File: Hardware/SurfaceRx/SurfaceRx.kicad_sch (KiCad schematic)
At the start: 29 parts, among them IC1 SC189ZSKTRT, J1 Conn_01x03, J2 Conn_01x03, J3 Conn_01x03, J4 Conn_01x03, J5 Conn_01x03, J6 Conn_01x03, J7 Conn_01x05, J8 Conn_01x03, P1 VDD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

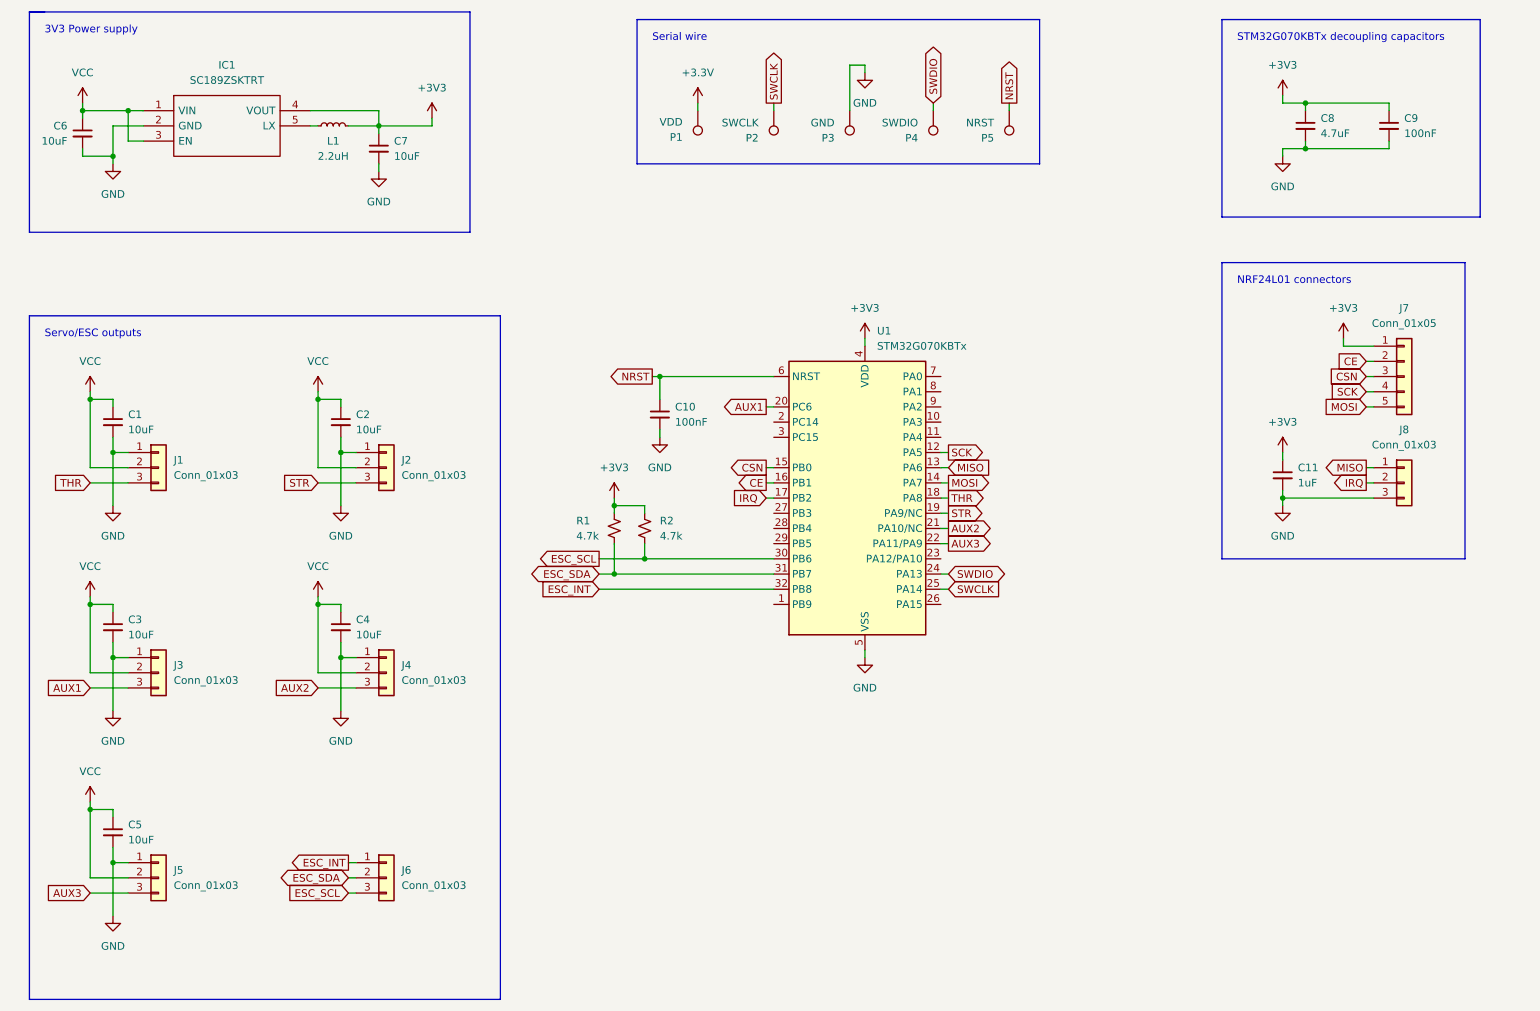
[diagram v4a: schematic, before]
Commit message: Added EEPROM to schematic
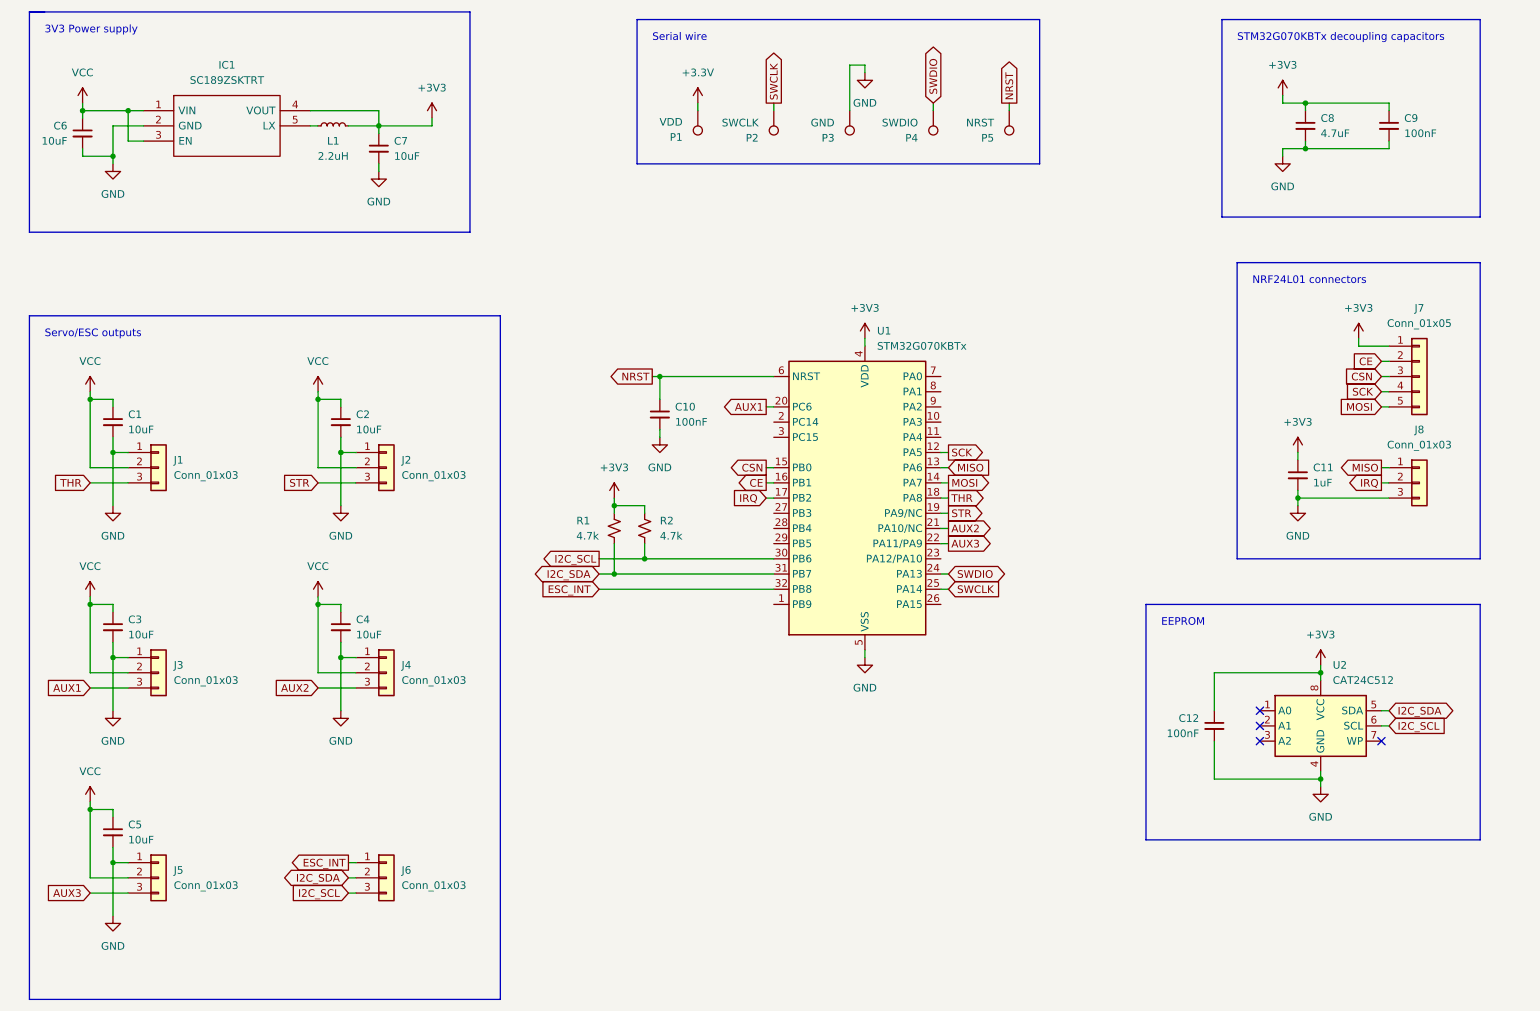
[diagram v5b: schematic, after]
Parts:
- added C12: 100nF, Capacitor_SMD:C_0603_1608Metric, symbol Device:C_Small
- added U2: CAT24C512, Package_SO:TSSOP-8_4.4x3mm_P0.65mm, symbol Custom_SurfaceRx:CAT24C512
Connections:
- net +3V3: now also C12.1, U2.8 (VCC)
- net GND: now also C12.2, U2.4 (GND)
- net ESC_SCL renamed I2C_SCL
- net I2C_SCL: now also U2.6 (SCL)
- net ESC_SDA renamed I2C_SDA
- net I2C_SDA: now also U2.5 (SDA)
- no-connect marks 0 -> 4
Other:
- note added: "EEPROM"
- moved on the sheet: C11, J7, J8

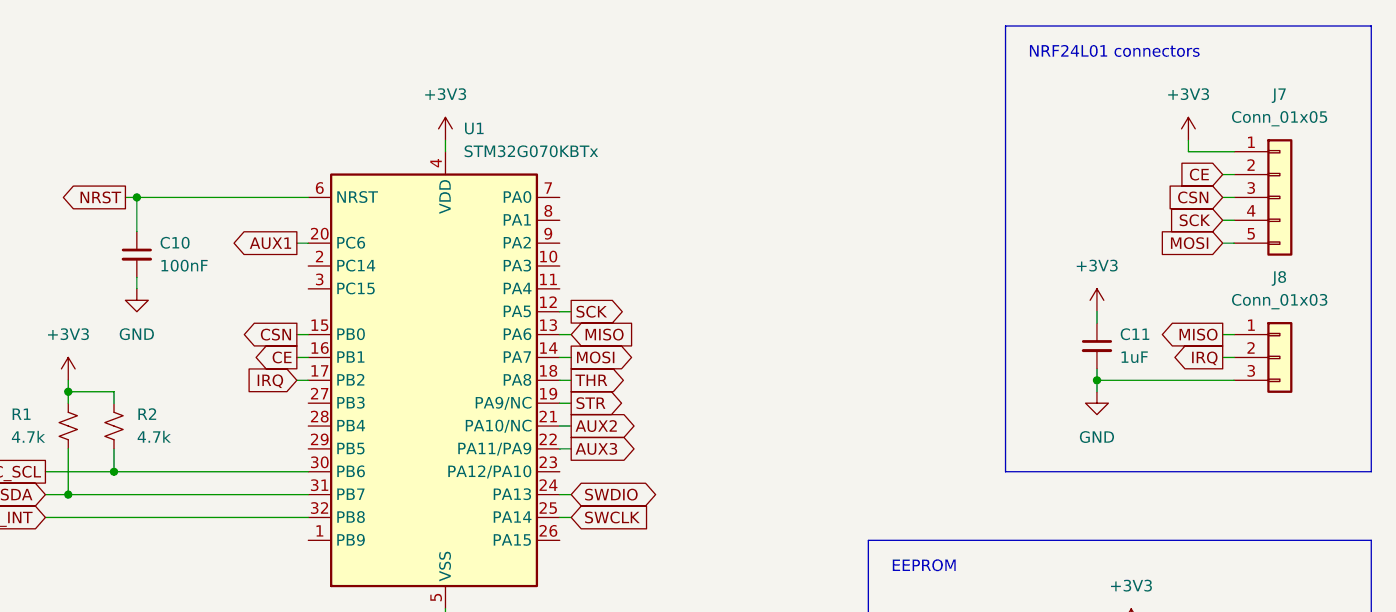
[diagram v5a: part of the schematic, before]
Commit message: Modified labels for clarity
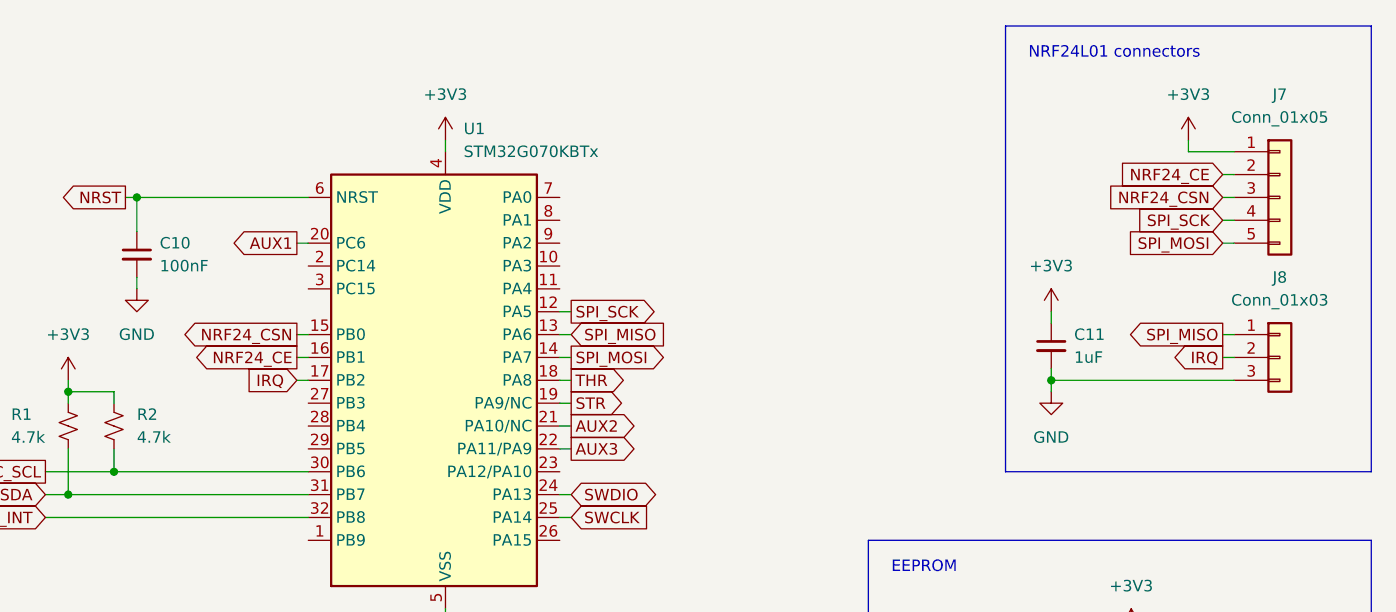
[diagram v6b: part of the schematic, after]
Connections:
- net CE renamed NRF24_CE
- net CSN renamed NRF24_CSN
- net MISO renamed SPI_MISO
- net MOSI renamed SPI_MOSI
- net SCK renamed SPI_SCK
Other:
- moved on the sheet: C11
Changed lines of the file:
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@@
   (junction (at 30.48 36.83) (diameter 0) (color 0 0 0 0)
   )
-  (junction (at 233.68 101.6) (diameter 0) (color 0 0 0 0)
+  (junction (at 228.6 101.6) (diameter 0) (color 0 0 0 0)
   )
   (junction (at 124.46 111.76) (diameter 0) (color 0 0 0 0)
@@
     (stroke (width 0) (type default) (color 0 0 0 0))
   )
-  (wire (pts (xy 233.68 101.6) (xy 248.92 101.6))
+  (wire (pts (xy 228.6 101.6) (xy 248.92 101.6))
     (stroke (width 0) (type default) (color 0 0 0 0))
   )
@@
     (stroke (width 0) (type default) (color 0 0 0 0))
   )
-  (wire (pts (xy 233.68 101.6) (xy 233.68 102.87))
+  (wire (pts (xy 228.6 101.6) (xy 228.6 102.87))
     (stroke (width 0) (type default) (color 0 0 0 0))
   )
@@
     (stroke (width 0) (type default) (color 0 0 0 0))
   )
-  (wire (pts (xy 233.68 93.98) (xy 233.68 95.25))
+  (wire (pts (xy 228.6 93.98) (xy 228.6 95.25))
     (stroke (width 0) (type default) (color 0 0 0 0))
   )
@@
     (stroke (width 0) (type solid) (color 0 0 0 0))
   )
-  (wire (pts (xy 233.68 100.33) (xy 233.68 101.6))
+  (wire (pts (xy 228.6 100.33) (xy 228.6 101.6))
     (stroke (width 0) (type default) (color 0 0 0 0))
   )
@@
     )
   )
-  (global_label "CE" (shape input) (at 247.65 78.74 180) (fields_autoplaced)
+  (global_label "NRF24_CE" (shape input) (at 247.65 78.74 180) (fields_autoplaced)
     (effects (font (size 1.27 1.27)) (justify right))
     (property "Intersheet References" "${INTERSHEET_REFS}" (id 0) (at 242.8179 78.6606 0)
@@
     )
   )
-  (global_label "CE" (shape output) (at 144.78 99.06 180) (fields_autoplaced)
+  (global_label "NRF24_CE" (shape output) (at 144.78 99.06 180) (fields_autoplaced)
     (effects (font (size 1.27 1.27)) (justify right))
     (property "Intersheet References" "${INTERSHEET_REFS}" (id 0) (at 139.9479 98.9806 0)
@@
     )
   )
-  (global_label "MOSI" (shape input) (at 247.65 86.36 180) (fields_autoplaced)
+  (global_label "SPI_MOSI" (shape input) (at 247.65 86.36 180) (fields_autoplaced)
     (effects (font (size 1.27 1.27)) (justify right))
     (property "Intersheet References" "${INTERSHEET_REFS}" (id 0) (at 240.6407 86.2806 0)
@@
     )
   )
-  (global_label "MISO" (shape input) (at 175.26 96.52 0) (fields_autoplaced)
+  (global_label "SPI_MISO" (shape input) (at 175.26 96.52 0) (fields_autoplaced)
     (effects (font (size 1.27 1.27)) (justify left))
     (property "Intersheet References" "${INTERSHEET_REFS}" (id 0) (at 182.2693 96.4406 0)
@@
     )
   )
-  (global_label "MISO" (shape output) (at 247.65 96.52 180) (fields_autoplaced)
+  (global_label "SPI_MISO" (shape output) (at 247.65 96.52 180) (fields_autoplaced)
     (effects (font (size 1.27 1.27)) (justify right))
     (property "Intersheet References" "${INTERSHEET_REFS}" (id 0) (at 240.6407 96.4406 0)
@@
     )
   )
-  (global_label "CSN" (shape output) (at 144.78 96.52 180) (fields_autoplaced)
+  (global_label "NRF24_CSN" (shape output) (at 144.78 96.52 180) (fields_autoplaced)
     (effects (font (size 1.27 1.27)) (justify right))
     (property "Intersheet References" "${INTERSHEET_REFS}" (id 0) (at 138.5569 96.4406 0)
@@
     )
   )
-  (global_label "SCK" (shape input) (at 247.65 83.82 180) (fields_autoplaced)
+  (global_label "SPI_SCK" (shape input) (at 247.65 83.82 180) (fields_autoplaced)
     (effects (font (size 1.27 1.27)) (justify right))
     (property "Intersheet References" "${INTERSHEET_REFS}" (id 0) (at 241.4874 83.7406 0)
@@
     )
   )
-  (global_label "SCK" (shape output) (at 175.26 93.98 0) (fields_autoplaced)
+  (global_label "SPI_SCK" (shape output) (at 175.26 93.98 0) (fields_autoplaced)
     (effects (font (size 1.27 1.27)) (justify left))
     (property "Intersheet References" "${INTERSHEET_REFS}" (id 0) (at 181.4226 93.9006 0)
@@
     )
   )
-  (global_label "CSN" (shape input) (at 247.65 81.28 180) (fields_autoplaced)
+  (global_label "NRF24_CSN" (shape input) (at 247.65 81.28 180) (fields_autoplaced)
     (effects (font (size 1.27 1.27)) (justify right))
     (property "Intersheet References" "${INTERSHEET_REFS}" (id 0) (at 241.4269 81.2006 0)
@@
     )
   )
-  (global_label "MOSI" (shape output) (at 175.26 99.06 0) (fields_autoplaced)
+  (global_label "SPI_MOSI" (shape output) (at 175.26 99.06 0) (fields_autoplaced)
     (effects (font (size 1.27 1.27)) (justify left))
     (property "Intersheet References" "${INTERSHEET_REFS}" (id 0) (at 182.2693 98.9806 0)
@@
     (pin "2")
   )
-  (symbol (lib_id "power:+3V3") (at 233.68 93.98 0) (unit 1)
-    (in_bom yes) (on_board yes) (fields_autoplaced)
-    (property "Reference" "#PWR022" (id 0) (at 233.68 97.79 0)
-      (effects (font (size 1.27 1.27)) hide)
-    )
-    (property "Value" "+3V3" (id 1) (at 233.68 88.9 0))
-    (property "Footprint" "" (id 2) (at 233.68 93.98 0)
-      (effects (font (size 1.27 1.27)) hide)
-    )
-    (property "Datasheet" "" (id 3) (at 233.68 93.98 0)
+  (symbol (lib_id "power:+3V3") (at 228.6 93.98 0) (unit 1)
+    (in_bom yes) (on_board yes) (fields_autoplaced)
+    (property "Reference" "#PWR022" (id 0) (at 228.6 97.79 0)
+      (effects (font (size 1.27 1.27)) hide)
+    )
+    (property "Value" "+3V3" (id 1) (at 228.6 88.9 0))
+    (property "Footprint" "" (id 2) (at 228.6 93.98 0)
+      (effects (font (size 1.27 1.27)) hide)
+    )
+    (property "Datasheet" "" (id 3) (at 228.6 93.98 0)
       (effects (font (size 1.27 1.27)) hide)
     )
@@
     (pin "1")
   )
-  (symbol (lib_id "Device:C_Small") (at 233.68 97.79 0) (unit 1)
-    (in_bom yes) (on_board yes) (fields_autoplaced)
-    (property "Reference" "C11" (id 0) (at 236.22 96.5262 0)
-      (effects (font (size 1.27 1.27)) (justify left))
-    )
-    (property "Value" "1uF" (id 1) (at 236.22 99.0662 0)
-      (effects (font (size 1.27 1.27)) (justify left))
-    )
-    (property "Footprint" "Capacitor_SMD:C_0603_1608Metric" (id 2) (at 233.68 97.79 0)
-      (effects (font (size 1.27 1.27)) hide)
-    )
-    (property "Datasheet" "~" (id 3) (at 233.68 97.79 0)
+  (symbol (lib_id "Device:C_Small") (at 228.6 97.79 0) (unit 1)
+    (in_bom yes) (on_board yes) (fields_autoplaced)
+    (property "Reference" "C11" (id 0) (at 231.14 96.5262 0)
+      (effects (font (size 1.27 1.27)) (justify left))
+    )
+    (property "Value" "1uF" (id 1) (at 231.14 99.0662 0)
+      (effects (font (size 1.27 1.27)) (justify left))
+    )
+    (property "Footprint" "Capacitor_SMD:C_0603_1608Metric" (id 2) (at 228.6 97.79 0)
+      (effects (font (size 1.27 1.27)) hide)
+    )
+    (property "Datasheet" "~" (id 3) (at 228.6 97.79 0)
       (effects (font (size 1.27 1.27)) hide)
     )
@@
     (pin "2")
   )
-  (symbol (lib_id "power:GND") (at 233.68 102.87 0) (unit 1)
-    (in_bom yes) (on_board yes) (fields_autoplaced)
-    (property "Reference" "#PWR023" (id 0) (at 233.68 109.22 0)
-      (effects (font (size 1.27 1.27)) hide)
-    )
-    (property "Value" "GND" (id 1) (at 233.68 107.95 0))
-    (property "Footprint" "" (id 2) (at 233.68 102.87 0)
-      (effects (font (size 1.27 1.27)) hide)
-    )
-    (property "Datasheet" "" (id 3) (at 233.68 102.87 0)
-      (effects (font (size 1.27 1.27)) hide)
-    )
+  (symbol (lib_id "power:GND") (at 228.6 102.87 0) (unit 1)
+    (in_bom yes) (on_board yes) (fields_autoplaced)
+    (property "Reference" "#PWR023" (id 0) (at 228.6 109.22 0)
+      (effects (font (size 1.27 1.27)) hide)
+    )
+    (property "Value" "GND" (id 1) (at 228.6 107.95 0))
+    (property "Footprint" "" (id 2) (at 228.6 102.87 0)
+      (effects (font (size 1.27 1.27)) hide)
+    )
+    (property "Datasheet" "" (id 3) (at 228.6 102.87 0)
+      (effects (font (size 1.27 1.27)) hide)
+    )

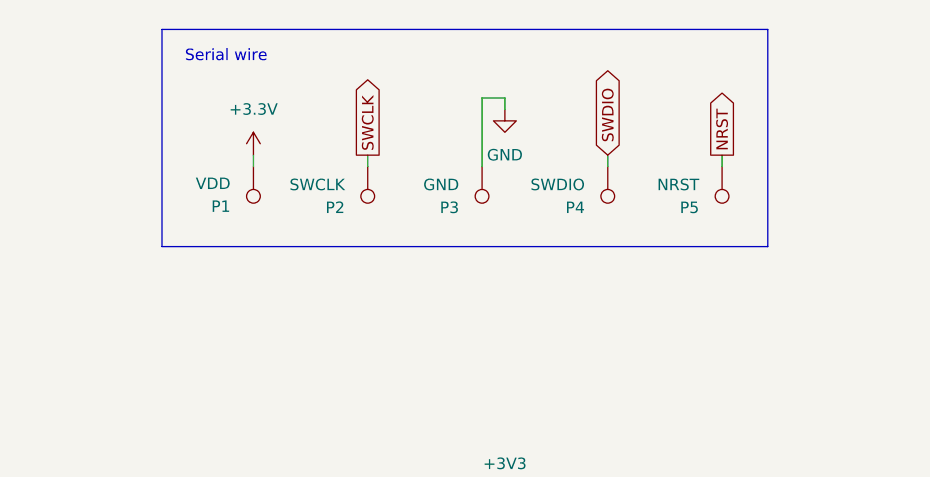
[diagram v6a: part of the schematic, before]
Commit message: Replaced debug pads with single header
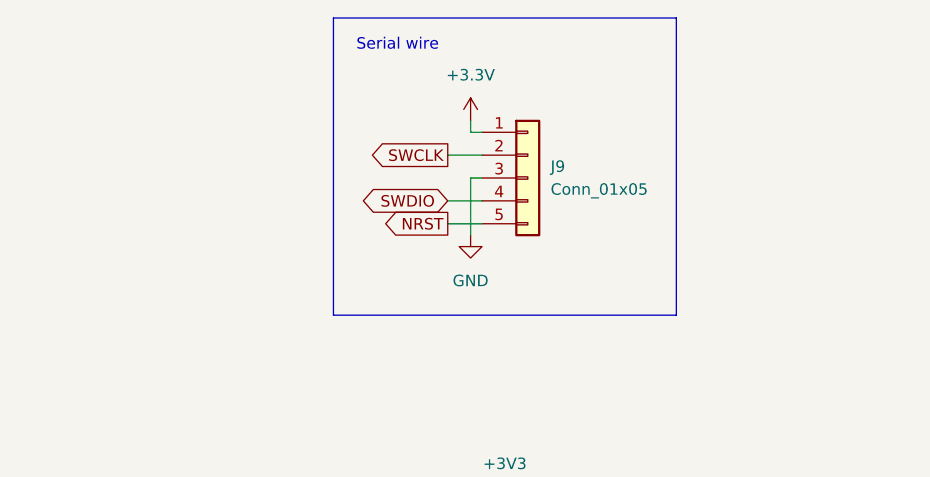
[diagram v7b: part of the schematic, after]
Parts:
- removed P1: VDD, TestPoint:TestPoint_Pad_D1.5mm, symbol Connector:TestPoint
- removed P2: SWCLK, TestPoint:TestPoint_Pad_D1.5mm, symbol Connector:TestPoint
- removed P3: GND, TestPoint:TestPoint_Pad_D1.5mm, symbol Connector:TestPoint
- removed P4: SWDIO, TestPoint:TestPoint_Pad_D1.5mm, symbol Connector:TestPoint
- removed P5: NRST, TestPoint:TestPoint_Pad_D1.5mm, symbol Connector:TestPoint
- added J9: Conn_01x05, Connector_PinHeader_2.54mm:PinHeader_1x05_P2.54mm_Vertical, symbol Connector_Generic:Conn_01x05
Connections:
- net +3.3V: now also J9.1 (Pin_1)
- net GND: now also J9.3 (Pin_3)
- net NRST: now also J9.5 (Pin_5)
- net SWCLK: now also J9.2 (Pin_2)
- net SWDIO: now also J9.4 (Pin_4)
